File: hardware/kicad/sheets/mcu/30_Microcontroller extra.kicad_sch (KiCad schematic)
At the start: 15 parts, among them U183 Teensy4.0, U191 CH343P

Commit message: reorganized
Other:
- title: Microcontroller extra -> MCU Auxiliary IO
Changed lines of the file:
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@@
 	(paper "User" 423.54 245.74)
 	(title_block
-		(title "Microcontroller extra")
+		(title "MCU Auxiliary IO")
 		(date "2026-02-16")
 	)

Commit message: before final cleanup
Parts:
- U10: renamed from U183; footprint teensy:Teensy41 -> teensy:Teensy40_SMT
- renumbered C280 to C38, C281 to C39, C284 to C40, C282 to C41, C285 to C42, C286 to C43, D82 to D22, D78 to D23, D79 to D24, L7 to L1, R519 to R74, R518 to R75, U191 to U11
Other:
- moved on the sheet: C40, C41

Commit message: added better footprints and steps
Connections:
- net SCL_FAST: now also U10.26 (19_A5_SCL0); no longer U10.35 (24_A10_TX6_SCL2)
- net SDA_FAST: now also U10.25 (18_A4_SDA0); no longer U10.36 (25_A11_RX6_SDA2)
- no-connect marks 22 -> 20

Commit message: better sheet nesting for power rails
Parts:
- removed C38: 47uF, Capacitor_SMD:C_0805_2012Metric, symbol 5v rail sm-easyedapro:GRM21BR61A476ME15L
- removed C39, C40, C42: 100nF, Capacitor_SMD:C_0603_1608Metric, symbol 5v rail sm-easyedapro:CC0603KRX7R9BB104
- removed C41, C43: 1uF, Capacitor_SMD:C_0603_1608Metric, symbol 5v rail sm-easyedapro:CL10B105KB8NQNC
- removed D22: TPD4E02B04DQAR, 5v rail sm-easyedapro:USON-10_L2.5-W1.0-P0.50-BL, symbol 5v rail sm-easyedapro:TPD4E02B04DQAR
- removed D23, D24: SS36, Diode_SMD:SMA, symbol 5v rail sm-easyedapro:SS36_C727061
- removed L1: BLM18AG601SN1D, Inductor_SMD:L_0603_1608Metric, symbol 5v rail sm-easyedapro:BLM18AG601SN1D
- removed R74, R75: 5.1kΩ, Resistor_SMD:R_0603_1608Metric, symbol 5v rail sm-easyedapro:FRC0603F5101TS
- removed U11: CH343P, Package_DFN_QFN:QFN-16-1EP_3x3mm_P0.5mm_EP1.7x1.7mm, symbol 5v rail sm-easyedapro:CH343P
- removed USB1: TYPE-C 16PIN 2MD(073), 5v rail sm-easyedapro:USB-C-SMD_TYPE-C-6PIN-2MD-073, symbol 5v rail sm-easyedapro:TYPE-C 16PIN 2MD(073)
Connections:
- net GND: no longer U10.32 (GND)
- no-connect marks 20 -> 7

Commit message: resheeted bms and fixed links for the 12v buck
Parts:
- renumbered U10 to U27
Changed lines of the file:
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@@
 		(on_board yes)
 		(dnp no)
-		(property "Reference" "U10"
+		(property "Reference" "U27"
 			(at 107.95 177.8 0)
 			(effects
@@
 			(project "svea_powerboard_rev3"
 				(path "/3f85abf4-0b95-4c4a-b7e9-06f59ca1ea3d/5c2e021f-c2d4-49e2-8c36-9a64f1f12004/8d05c3b8-20a4-4a7f-9b20-01f8d5d5be47"
-					(reference "U10")
+					(reference "U27")
 					(unit 1)
 				)
@@
 		(on_board yes)
 		(dnp no)
-		(property "Reference" "#PWR0141"
+		(property "Reference" "#PWR093"
 			(at 16.51 194.31 0)
 			(effects
@@
 			(project "svea_powerboard_rev3"
 				(path "/3f85abf4-0b95-4c4a-b7e9-06f59ca1ea3d/5c2e021f-c2d4-49e2-8c36-9a64f1f12004/8d05c3b8-20a4-4a7f-9b20-01f8d5d5be47"
-					(reference "#PWR0141")
+					(reference "#PWR093")
 					(unit 1)
 				)
@@
 		(on_board yes)
 		(dnp no)
-		(property "Reference" "#PWR0151"
+		(property "Reference" "#PWR097"
 			(at 198.12 173.99 0)
 			(effects
@@
 			(project "svea_powerboard_rev3"
 				(path "/3f85abf4-0b95-4c4a-b7e9-06f59ca1ea3d/5c2e021f-c2d4-49e2-8c36-9a64f1f12004/8d05c3b8-20a4-4a7f-9b20-01f8d5d5be47"
-					(reference "#PWR0151")
+					(reference "#PWR097")
 					(unit 1)
 				)

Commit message: various improvements
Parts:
- renumbered U27 to U45
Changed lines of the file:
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@@
 		(on_board yes)
 		(dnp no)
-		(property "Reference" "U27"
+		(property "Reference" "U45"
 			(at 107.95 177.8 0)
 			(effects
@@
 			(project "svea_powerboard_rev3"
 				(path "/3f85abf4-0b95-4c4a-b7e9-06f59ca1ea3d/5c2e021f-c2d4-49e2-8c36-9a64f1f12004/8d05c3b8-20a4-4a7f-9b20-01f8d5d5be47"
-					(reference "U27")
+					(reference "U45")
 					(unit 1)
 				)
@@
 		(on_board yes)
 		(dnp no)
-		(property "Reference" "#PWR093"
+		(property "Reference" "#PWR0144"
 			(at 16.51 194.31 0)
 			(effects
@@
 			(project "svea_powerboard_rev3"
 				(path "/3f85abf4-0b95-4c4a-b7e9-06f59ca1ea3d/5c2e021f-c2d4-49e2-8c36-9a64f1f12004/8d05c3b8-20a4-4a7f-9b20-01f8d5d5be47"
-					(reference "#PWR093")
+					(reference "#PWR0144")
 					(unit 1)
 				)
@@
 		(on_board yes)
 		(dnp no)
-		(property "Reference" "#PWR097"
+		(property "Reference" "#PWR0145"
 			(at 198.12 173.99 0)
 			(effects
@@
 			(project "svea_powerboard_rev3"
 				(path "/3f85abf4-0b95-4c4a-b7e9-06f59ca1ea3d/5c2e021f-c2d4-49e2-8c36-9a64f1f12004/8d05c3b8-20a4-4a7f-9b20-01f8d5d5be47"
-					(reference "#PWR097")
+					(reference "#PWR0145")
 					(unit 1)
 				)

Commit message: various improvements
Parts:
- renumbered U45 to U48
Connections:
- net MCU-PIN-IC-INT: no longer names the net of U48.6 (4_BCLK2)
- net SBUS_RECEIVER: no longer names the net of U48.9 (7_RX2_OUT1A)
- net SCL_SLOW: no longer names the net of U48.23 (16_A2_RX4_SCL1)
- net SDA_SLOW: no longer names the net of U48.24 (17_A3_TX4_SDA1)
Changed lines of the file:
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@@
-		)
-	)
-	(global_label "SCL_SLOW"
-		(shape input)
-		(at 67.31 196.85 180)
-		(effects
-			(font
-				(size 1.5748 1.5748)
-			)
-			(justify right)
-		)
-		(property "Intersheetrefs" "${INTERSHEET_REFS}"
-			(at 67.31 196.85 0)
-			(effects
-				(font
-					(size 1.27 1.27)
-				)
-				(hide yes)
-			)
-		)
-	)
-	(global_label "SBUS_RECEIVER"
-		(shape input)
-		(at 76.2 163.83 180)
-		(effects
-			(font
-				(size 1.5748 1.5748)
-			)
-			(justify right)
-		)
-		(property "Intersheetrefs" "${INTERSHEET_REFS}"
-			(at 76.2 163.83 0)
-			(effects
-				(font
-					(size 1.27 1.27)
-				)
-				(hide yes)
-			)
-		)
-	)
-	(global_label "SDA_SLOW"
-		(shape input)
-		(at 67.31 200.66 180)
-		(effects
-			(font
-				(size 1.5748 1.5748)
-			)
-			(justify right)
-		)
-		(property "Intersheetrefs" "${INTERSHEET_REFS}"
-			(at 67.31 200.66 0)
-			(effects
-				(font
-					(size 1.27 1.27)
-				)
-				(hide yes)
-			)
-		)
-	)
-	(global_label "MCU-PIN-IC-INT"
-		(shape input)
-		(at 76.2 156.21 180)
-		(effects
-			(font
-				(size 1.5748 1.5748)
-			)
-			(justify right)
-		)
-		(property "Intersheetrefs" "${INTERSHEET_REFS}"
-			(at 76.2 156.21 0)
-			(effects
-				(font
-					(size 1.27 1.27)
-				)
-				(hide yes)
-			)
 		)
 	)
@@
 		(on_board yes)
 		(dnp no)
-		(property "Reference" "U45"
+		(property "Reference" "U48"
 			(at 107.95 177.8 0)
 			(effects
@@
 			(project "svea_powerboard_rev3"
 				(path "/3f85abf4-0b95-4c4a-b7e9-06f59ca1ea3d/5c2e021f-c2d4-49e2-8c36-9a64f1f12004/8d05c3b8-20a4-4a7f-9b20-01f8d5d5be47"
-					(reference "U45")
+					(reference "U48")
 					(unit 1)
 				)
@@
 		(on_board yes)
 		(dnp no)
-		(property "Reference" "#PWR0144"
+		(property "Reference" "#PWR0155"
 			(at 16.51 194.31 0)
 			(effects
@@
 			(project "svea_powerboard_rev3"
 				(path "/3f85abf4-0b95-4c4a-b7e9-06f59ca1ea3d/5c2e021f-c2d4-49e2-8c36-9a64f1f12004/8d05c3b8-20a4-4a7f-9b20-01f8d5d5be47"
-					(reference "#PWR0144")
+					(reference "#PWR0155")
 					(unit 1)
 				)
@@
 		(on_board yes)
 		(dnp no)
-		(property "Reference" "#PWR0145"
+		(property "Reference" "#PWR0156"
 			(at 198.12 173.99 0)
 			(effects
@@
 			(project "svea_powerboard_rev3"
 				(path "/3f85abf4-0b95-4c4a-b7e9-06f59ca1ea3d/5c2e021f-c2d4-49e2-8c36-9a64f1f12004/8d05c3b8-20a4-4a7f-9b20-01f8d5d5be47"
-					(reference "#PWR0145")
+					(reference "#PWR0156")
 					(unit 1)
 				)

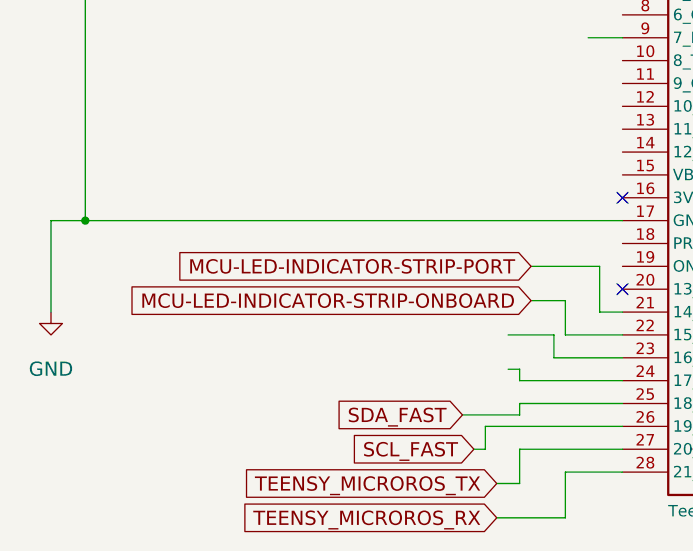
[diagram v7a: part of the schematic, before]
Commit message: current sensing on the servos and cleaning up empty sheets
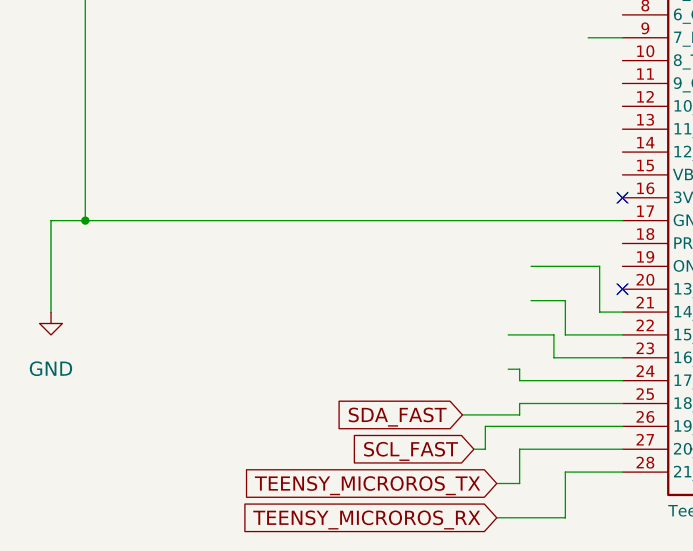
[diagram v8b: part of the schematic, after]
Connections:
- net MCU-LED-INDICATOR-STRIP-ONBOARD: no longer names the net of U48.22 (15_A1_RX3_SPDIF_IN)
- net MCU-LED-INDICATOR-STRIP-PORT: no longer names the net of U48.21 (14_A0_TX3_SPDIF_OUT)
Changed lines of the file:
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@@
-		)
-	)
-	(global_label "MCU-LED-INDICATOR-STRIP-ONBOARD"
-		(shape input)
-		(at 69.85 193.04 180)
-		(effects
-			(font
-				(size 1.5748 1.5748)
-			)
-			(justify right)
-		)
-		(property "Intersheetrefs" "${INTERSHEET_REFS}"
-			(at 69.85 193.04 0)
-			(effects
-				(font
-					(size 1.27 1.27)
-				)
-				(hide yes)
-			)
 		)
 	)
@@
 			(effects
 				(font
-					(size 1.27 1.27)
-				)
-				(hide yes)
-			)
-		)
-	)
-	(global_label "MCU-LED-INDICATOR-STRIP-PORT"
-		(shape input)
-		(at 69.85 189.23 180)
-		(effects
-			(font
-				(size 1.5748 1.5748)
-			)
-			(justify right)
-		)
-		(property "Intersheetrefs" "${INTERSHEET_REFS}"
-			(at 69.85 189.23 0)
-			(effects
-				(font
